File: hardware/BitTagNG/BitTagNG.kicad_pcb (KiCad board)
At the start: 2 copper layers, 17.2 x 9 mm, 22 parts, among them J201 CONN_02X04, J301 Conn_01x01, J302 Conn_01x01, J303 Conn_01x01, J304 Conn_01x01, J401 CONN_01X02, Q501 Q_NPN_BEC, U1 at25ex321D-UUN, U2 adxl367, U302 stm32l431kc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

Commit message: update decoupling for adxl367
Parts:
- added R2: 10, Resistor_SMD:R_0201_0603Metric, F.Cu at (145.5, 106.1)
- moved C404 4.01 mm to (148.8, 105.0)
- moved C503 0.95 mm to (146.8, 108.3)
- moved C5 0.75 mm to (145.1, 107.2)
- moved C1 0.59 mm to (144.8, 106.1), turned to -90 degrees
- moved C3 0.50 mm to (145.1, 108.0), turned to 0 degrees
- moved C502 0.15 mm to (146.8, 105.4)
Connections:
- C1 pad 1: VIN -> Net-(C1-Pad1)
- U2 pad 12: VIN -> Net-(C1-Pad1)
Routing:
- net Net-(C1-Pad1): track 0.00 -> 1.73 mm
- net VIN: track 42.6 -> 41.7 mm
- net GND: track 50.8 -> 50.0 mm
- net Net-(C502-Pad1): track 9.50 -> 8.81 mm

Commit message: update bittagng
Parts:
- removed R2: 10, Resistor_SMD:R_0201_0603Metric
- moved C1 0.51 mm to (145.1, 106.5), turned to 0 degrees
- moved Q501 0.50 mm to (146.8, 106.8)
- moved C502 0.47 mm to (146.8, 105.8)
- moved U501 0.24 mm to (143.1, 110.7)
- moved R1 0.24 mm to (144.2, 109.1)
- moved C2 0.22 mm to (142.2, 109.1)
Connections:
- C1 pad 1: Net-(C1-Pad1) -> VIN
- U2 pad 12: Net-(C1-Pad1) -> VIN
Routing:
- net /WKUP4: track 3.10 -> 4.88 mm
- net Net-(C1-Pad1): track 1.73 -> 0.00 mm
- net GND: track 50.0 -> 51.4 mm
- net VIN: track 41.7 -> 42.3 mm

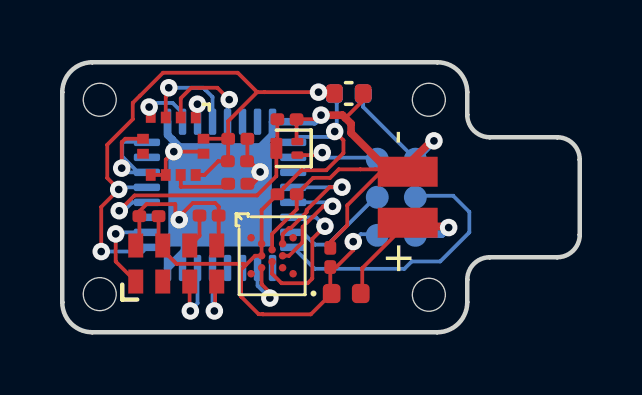
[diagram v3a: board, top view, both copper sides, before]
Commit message: optimize BitTagNG pcb
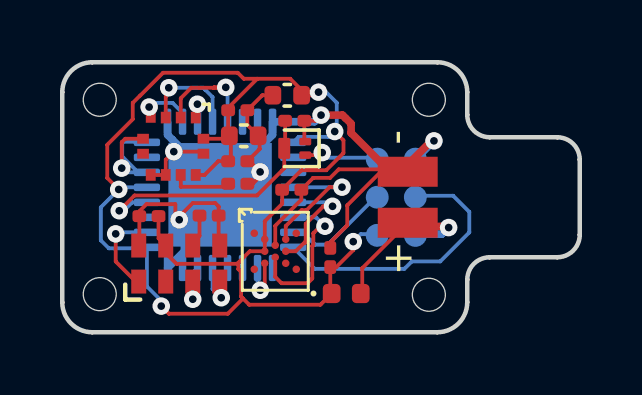
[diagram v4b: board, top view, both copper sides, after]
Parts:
- C4: moved to F.Cu
- moved C404 3.77 mm to (145.3, 106.4)
- moved C4 2.05 mm to (146.8, 105.0), turned to 180 degrees
- moved C5 1.70 mm to (145.1, 105.5)
- moved C1 0.75 mm to (145.1, 107.2)
- moved C502 0.26 mm to (147.0, 105.9)
- moved Q501 0.26 mm to (147.0, 106.8)
- moved C503 0.22 mm to (146.9, 108.2)
- moved U1 0.18 mm to (146.4, 110.2)
- moved U501 0.10 mm to (143.2, 110.7)
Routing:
- net VIN: track 42.3 -> 46.9 mm
- net GND: track 51.4 -> 49.4 mm
- net /AT25_SCK: track 2.30 -> 1.74 mm
- net /SCL: track 2.20 -> 1.70 mm

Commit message: reduced via/track sizes for BitTagNG
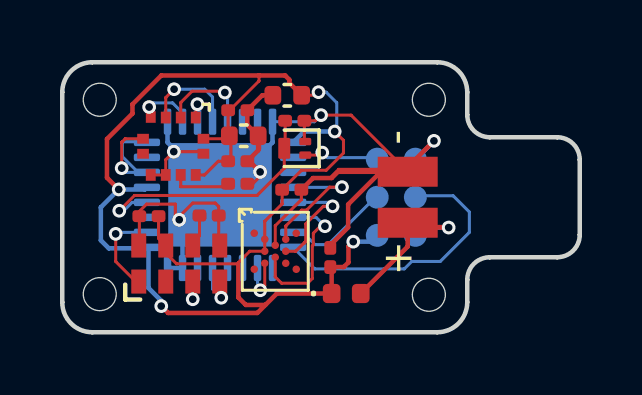
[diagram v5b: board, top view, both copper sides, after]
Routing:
- net VIN: track 46.9 -> 48.6 mm
- net VBAT: track 6.13 -> 7.34 mm
- net GND: track 49.4 -> 48.6 mm
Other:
- board text added: "BTNG V2"
- board text removed: "BTNG V1"

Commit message: added capacitor to BitTagNG
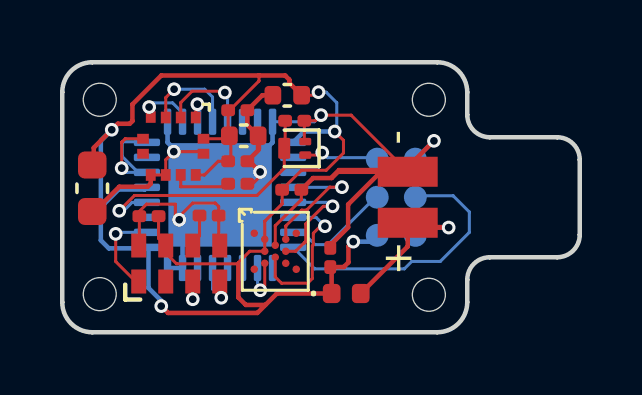
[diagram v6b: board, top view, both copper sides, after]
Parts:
- added C6: 47uf, Capacitor_SMD:C_0603_1608Metric, F.Cu at (140.3, 108.1)
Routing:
- net GND: track 48.6 -> 51.1 mm
- net VIN: track 48.6 -> 50.6 mm
